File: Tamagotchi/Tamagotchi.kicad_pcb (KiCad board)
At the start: 4 copper layers, 40 x 54.9 mm, 78 parts, among them J1 CH_USB_C, J2 display: GMT085-01, J3 JTAG, Q1 ZVP1320FTA, Q2 SS8050-MS, SW1 A, SW2 B, SW3 C, SW4 BOOT, SW5 NRST, U1 MCP73833, U2 STM32U031K4Ux, U3 AT25EU0021A-MAHN-T, U4 AP7343D-33W5, Y1 32.786KHz

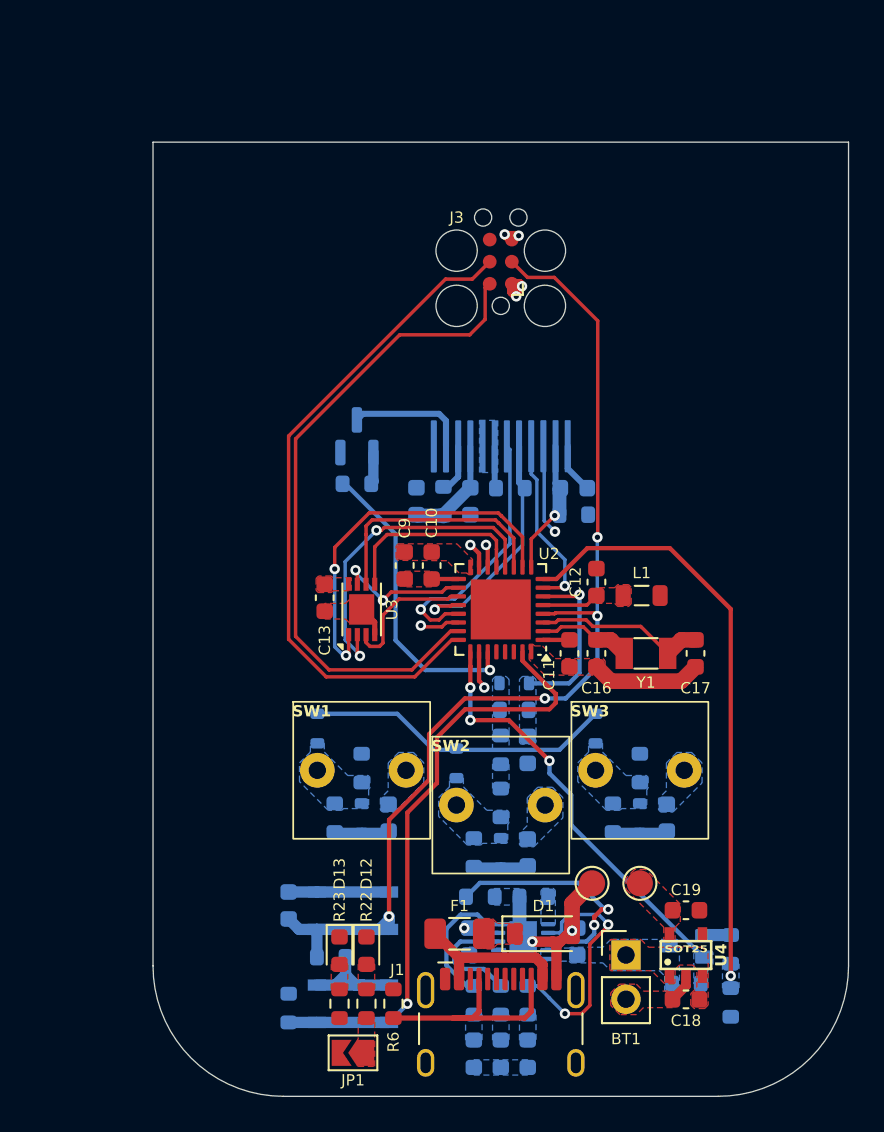
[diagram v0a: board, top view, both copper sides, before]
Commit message: Fixed power section
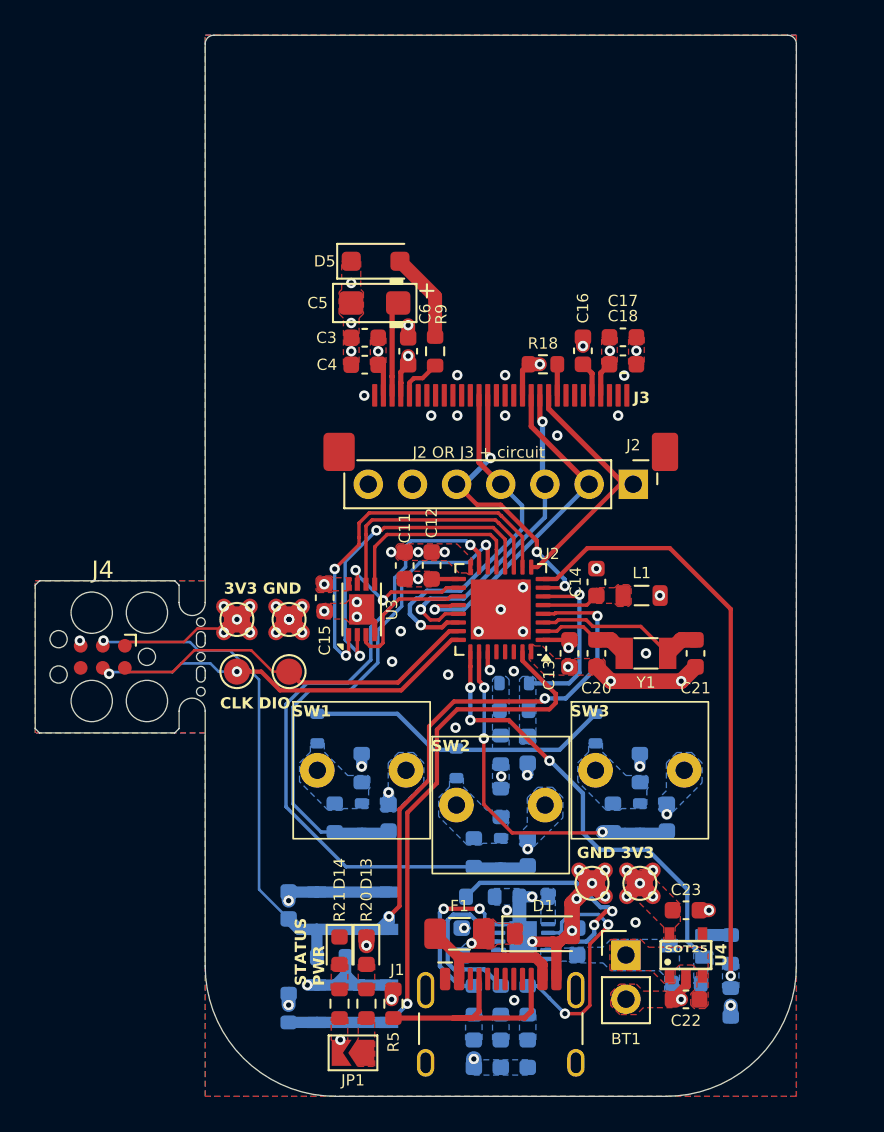
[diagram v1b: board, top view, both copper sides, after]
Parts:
- removed the C14 at (154.2, 93.0)
- removed Q2: SS8050-MS, Package_TO_SOT_SMD:SOT-23
- removed the R10 at (146.7, 93.8)
- removed the R19 at (154.2, 94.5)
- removed the R20 at (150.6, 93.0)
- added C16: 1u, Capacitor_SMD:C_0603_1608Metric, F.Cu at (154.7, 85.1)
- added C17: 4u7, Capacitor_SMD:C_0603_1608Metric, F.Cu at (157.0, 84.3)
- added C18: 100n, Capacitor_SMD:C_0603_1608Metric, F.Cu at (157.0, 85.9)
- added C5: 4u7, PCM_Capacitor_Tantalum_SMD_AKL:CP_EIA-3216-18_Kemet-A, F.Cu at (142.8, 82.4)
- added C6: 1u, Capacitor_SMD:C_0603_1608Metric, F.Cu at (144.7, 85.2)
- added D5: USL1G, Diode_SMD:D_SOD-123F, F.Cu at (142.8, 80.0)
- added J4: JTAG, Connector:Tag-Connect_TC2030-IDC-FP_2x03_P1.27mm_Vertical, F.Cu at (127.1, 102.7)
- added R18: 560k, Resistor_SMD:R_0603_1608Metric, F.Cu at (152.4, 85.9)
- added TP1: SWCLK, TestPoint:TestPoint_Pad_D1.5mm, F.Cu at (134.8, 103.6)
- added TP2: SWDIO, TestPoint:TestPoint_Pad_D1.5mm, F.Cu at (137.8, 103.6)
- added TP3: GND, TestPoint:TestPoint_Pad_D1.5mm, F.Cu at (137.8, 100.6)
- added TP4: 3v3, TestPoint:TestPoint_Pad_D1.5mm, F.Cu at (134.8, 100.6)
- C3: value 100n -> 10u; moved to F.Cu
- C4: moved to F.Cu
- J2: value display: GMT085-01 -> OLED_FB; footprint Marijn:GMT085-01 -> Connector_PinHeader_2.54mm:PinHeader_1x07_P2.54mm_Vertical; moved to F.Cu
- J3: value JTAG -> FFC2B35-30-T; footprint Connector:Tag-Connect_TC2030-IDC-FP_2x03_P1.27mm_Vertical -> Marijn:FFC2B35-30
- R9: value 2k2 -> 50r; moved to F.Cu
- moved C4 9.93 mm to (142.2, 85.9), turned to 0 degrees
- moved C3 9.86 mm to (142.2, 84.4), turned to 0 degrees
- moved J3 9.06 mm to (150.0, 89.1), turned to 0 degrees
- moved R9 8.85 mm to (146.2, 85.2), turned to 90 degrees
- moved J2 7.92 mm to (157.6, 92.8), turned to -90 degrees
- moved C2 0.43 mm to (147.8, 119.1)
- renumbered C8 to C10, C9 to C11, C10 to C12, C11 to C13, C12 to C14, C13 to C15, C15 to C19, C16 to C20, C17 to C21, C18 to C22, C19 to C23, C5 to C7, C6 to C8, C7 to C9, D9 to D10, D10 to D11, D11 to D12, D12 to D13, D13 to D14, D5 to D6, D6 to D7, D7 to D8, D8 to D9, R2 to R1, R11 to R10, R12 to R11, R13 to R12, R14 to R13, R15 to R14, R16 to R15, R17 to R16, R18 to R17, R21 to R19, R1 to R2, R22 to R20, R23 to R21, R24 to R22, R5 to R4, R6 to R5, R7 to R6, R4 to R7, TP1 to TP5, TP2 to TP6
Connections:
- C3 pad 1: +3V3 -> GND
- C3 pad 2: GND -> +3V3
- C4 pad 1: +3V3 -> GND
- C4 pad 2: GND -> +3V3
- J2 pad 1: GND -> /OLED_NRST
- J2 pad 2: Net-(J2-Pin_2) -> /OLED_SPI_NSS
- J2 pad 3: Net-(J2-Pin_3) -> /OLED_DC
- J2 pad 4: +3V3 -> /OLED_SPI_MOSI
- J2 pad 5: GND -> /OLED_SPI_SCK
- J2 pad 7: /TFT_DC -> +3V3
- J3 pad 1: +3V3 -> GND
- J3 pad 2: /SWDIO -> +3V3
- J3 pad 3: /NRST -> Net-(J3-Pin_3)
- J3 pad 4: /SWCLK -> +3V3
- J3 pad 5: GND -> /OLED_VSL
- R9 pad 1: Net-(Q2-B) -> /OLED_VSL
- R9 pad 2: /TFT_BL -> Net-(D5-A)
- U2 pad 20: /TFT_SPI_NSS -> /OLED_SPI_NSS
- U2 pad 21: /TFT_DC -> /OLED_DC
- U2 pad 22: /TFT_SPI_MOSI -> /OLED_SPI_MOSI
- U2 pad 27: /TFT_BL -> unconnected-(U2-PB4-Pad27)
- U2 pad 7: /TFT_SPI_SCK -> /OLED_SPI_SCK
- U2 pad 9: /TFT_NRST -> /OLED_NRST
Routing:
- net /B: track 4.66 -> 40.0 mm
- net GND: track 37.0 -> 69.6 mm, vias 5 -> 66
- net /A: track 4.55 -> 30.1 mm
- net /OLED_SPI_MOSI: track 0.00 -> 20.7 mm, vias 0 -> 1
- net /OLED_SPI_NSS: track 0.00 -> 19.8 mm, vias 0 -> 1
- net /OLED_DC: track 0.00 -> 19.2 mm, vias 0 -> 2
- net /TFT_BL: track 17.6 -> 0.00 mm, vias 1 -> 0
- net /TFT_SPI_MOSI: track 17.5 -> 0.00 mm, vias 2 -> 0
- net /OLED_SPI_SCK: track 0.00 -> 17.1 mm, vias 0 -> 3
- net /SWDIO: track 38.4 -> 21.8 mm
- net /SWCLK: track 38.9 -> 22.7 mm, vias 0 -> 2
- net +3V3: track 19.4 -> 35.4 mm, vias 2 -> 22
- net /OLED_NRST: track 0.00 -> 15.3 mm
- net /TFT_DC: track 15.0 -> 0.00 mm, vias 1 -> 0
- net /C: track 5.34 -> 20.2 mm, vias 1 -> 3
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- added copper zone on In2.Cu, net +3V3
- added copper zone on In1.Cu, net GND
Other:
- board size 40 x 54.9 mm -> 43.8 x 61 mm
- board text added: "3V3 GND"
- board text added: "BOOT"
- board text added: "CLK DIO"
- board text added: "FOLD"
- board text added: "GND 3V3"
- board text added: "J2 OR J3 + circuit"
- board text added: "NRST"
- board text added: "PG ST1 ST2"
- board text added: "STATUS PWR"
